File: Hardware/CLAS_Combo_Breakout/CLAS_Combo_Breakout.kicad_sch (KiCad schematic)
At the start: 86 parts, among them J1 USB_C_Receptacle_USB2.0, J2 ZED, J3 NEO, J4 USB_C_Receptacle_USB2.0, J5 Conn_SMA, U1 USBLC6-2P6, U10 NT1191GEAE3S, U2 ZED-F9P, U3 NEO-D9C-00B, U4 USBLC6-2P6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

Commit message: 部品配置を調整
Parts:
- JP1: footprint Jumper:SolderJumper-3_P1.3mm_Open_RoundedPad1.0x1.5mm_NumberLabels -> Jumper_extlib:SolderJumper-3_Open_RoundedPad
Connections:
- net D+ZED: now also U1.6 (I/O1); no longer U1.4 (I/O2)
- net D-ZED: now also U1.4 (I/O2); no longer U1.6 (I/O1)
- net RXD1_ZED: now also J2.6 (Pin_6); no longer J2.5 (Pin_5)
- net TXD1_ZED: now also J2.7 (Pin_7); no longer J2.6 (Pin_6)
- net TX_RDY: now also J2.5 (Pin_5); no longer J2.7 (Pin_7)
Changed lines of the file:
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@@
   (junction (at 43.18 160.02) (diameter 0) (color 0 0 0 0)
   )
-  (junction (at 264.16 43.18) (diameter 0) (color 0 0 0 0)
-  )
   (junction (at 242.57 144.78) (diameter 0) (color 0 0 0 0)
   )
@@
   (junction (at 267.97 144.78) (diameter 0) (color 0 0 0 0)
   )
+  (junction (at 264.16 40.64) (diameter 0) (color 0 0 0 0)
+  )
   (junction (at 35.56 40.64) (diameter 0) (color 0 0 0 0)
   )
+  (junction (at 256.54 43.18) (diameter 0) (color 0 0 0 0)
+  )
   (junction (at 283.21 85.09) (diameter 0) (color 0 0 0 0)
   )
@@
   (junction (at 133.35 68.58) (diameter 0) (color 0 0 0 0)
   )
-  (junction (at 256.54 40.64) (diameter 0) (color 0 0 0 0)
-  )
   (junction (at 267.97 154.94) (diameter 0) (color 0 0 0 0)
   )
@@
     (stroke (width 0) (type default) (color 0 0 0 0))
   )
-  (wire (pts (xy 264.16 43.18) (xy 264.16 44.45))
-    (stroke (width 0) (type default) (color 0 0 0 0))
-  )
   (wire (pts (xy 267.97 144.78) (xy 267.97 147.32))
     (stroke (width 0) (type default) (color 0 0 0 0))
@@
     (stroke (width 0) (type default) (color 0 0 0 0))
   )
+  (wire (pts (xy 256.54 43.18) (xy 256.54 44.45))
+    (stroke (width 0) (type default) (color 0 0 0 0))
+  )
+  (wire (pts (xy 264.16 40.64) (xy 266.7 40.64))
+    (stroke (width 0) (type default) (color 0 0 0 0))
+  )
   (wire (pts (xy 95.25 187.96) (xy 95.25 189.23))
     (stroke (width 0) (type default) (color 0 0 0 0))
@@
     (stroke (width 0) (type default) (color 0 0 0 0))
   )
-  (wire (pts (xy 251.46 43.18) (xy 264.16 43.18))
-    (stroke (width 0) (type default) (color 0 0 0 0))
-  )
   (wire (pts (xy 107.95 165.1) (xy 107.95 172.72))
     (stroke (width 0) (type default) (color 0 0 0 0))
@@
     (stroke (width 0) (type default) (color 0 0 0 0))
   )
-  (wire (pts (xy 264.16 43.18) (xy 266.7 43.18))
+  (wire (pts (xy 251.46 43.18) (xy 256.54 43.18))
     (stroke (width 0) (type default) (color 0 0 0 0))
   )
@@
     (stroke (width 0) (type default) (color 0 0 0 0))
   )
-  (wire (pts (xy 251.46 40.64) (xy 256.54 40.64))
+  (wire (pts (xy 251.46 40.64) (xy 264.16 40.64))
     (stroke (width 0) (type default) (color 0 0 0 0))
   )
@@
     (stroke (width 0) (type default) (color 0 0 0 0))
   )
+  (wire (pts (xy 256.54 43.18) (xy 266.7 43.18))
+    (stroke (width 0) (type default) (color 0 0 0 0))
+  )
   (wire (pts (xy 66.04 144.78) (xy 68.58 144.78))
     (stroke (width 0) (type default) (color 0 0 0 0))
@@
     (stroke (width 0) (type default) (color 0 0 0 0))
   )
-  (wire (pts (xy 256.54 40.64) (xy 266.7 40.64))
-    (stroke (width 0) (type default) (color 0 0 0 0))
-  )
   (wire (pts (xy 35.56 40.64) (xy 35.56 39.37))
     (stroke (width 0) (type default) (color 0 0 0 0))
@@
     (stroke (width 0) (type default) (color 0 0 0 0))
   )
+  (wire (pts (xy 264.16 40.64) (xy 264.16 44.45))
+    (stroke (width 0) (type default) (color 0 0 0 0))
+  )
   (wire (pts (xy 64.77 177.8) (xy 67.31 177.8))
     (stroke (width 0) (type default) (color 0 0 0 0))
@@
     (stroke (width 0) (type default) (color 0 0 0 0))
   )
-  (wire (pts (xy 256.54 40.64) (xy 256.54 44.45))
-    (stroke (width 0) (type default) (color 0 0 0 0))
-  )
   (wire (pts (xy 260.35 92.71) (xy 260.35 99.06))
     (stroke (width 0) (type default) (color 0 0 0 0))
@@
     (effects (font (size 1.27 1.27)) (justify right bottom))
   )
-  (label "TX_RDY" (at 177.8 77.47 180)
+  (label "TX_RDY" (at 177.8 72.39 180)
     (effects (font (size 1.27 1.27)) (justify right bottom))
   )
@@
     (effects (font (size 1.27 1.27)) (justify right bottom))
   )
-  (label "RXD1_ZED" (at 177.8 72.39 180)
+  (label "RXD1_ZED" (at 177.8 74.93 180)
     (effects (font (size 1.27 1.27)) (justify right bottom))
   )
@@
     (effects (font (size 1.27 1.27)) (justify left bottom))
   )
-  (label "TXD1_ZED" (at 177.8 74.93 180)
+  (label "TXD1_ZED" (at 177.8 77.47 180)
     (effects (font (size 1.27 1.27)) (justify right bottom))
   )
@@
     (property "Reference" "JP1" (id 0) (at 121.92 34.29 0))
     (property "Value" "I2C" (id 1) (at 121.92 31.75 0))
-    (property "Footprint" "Jumper:SolderJumper-3_P1.3mm_Open_RoundedPad1.0x1.5mm_NumberLabels" (id 2) (at 121.92 29.21 0)
+    (property "Footprint" "Jumper_extlib:SolderJumper-3_Open_RoundedPad" (id 2) (at 121.92 29.21 0)
       (effects (font (size 1.27 1.27)) hide)
     )
@@
     )
     (path "/b54126b3-7985-4549-85a9-fc253ef56032"
-      (reference "JP1") (unit 1) (value "I2C") (footprint "Jumper:SolderJumper-3_P1.3mm_Open_RoundedPad1.0x1.5mm_NumberLabels")
+      (reference "JP1") (unit 1) (value "I2C") (footprint "Jumper_extlib:SolderJumper-3_Open_RoundedPad")
     )
     (path "/be16f664-0619-4856-937a-e239b591adad"

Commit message: 配線中
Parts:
- removed C9: 0.1u, Capacitor_SMD:C_0603_1608Metric, symbol Device:C_Small
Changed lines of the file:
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@@
   (junction (at 40.64 190.5) (diameter 0) (color 0 0 0 0)
   )
-  (junction (at 267.97 144.78) (diameter 0) (color 0 0 0 0)
-  )
   (junction (at 264.16 40.64) (diameter 0) (color 0 0 0 0)
   )
@@
   (junction (at 133.35 68.58) (diameter 0) (color 0 0 0 0)
   )
-  (junction (at 267.97 154.94) (diameter 0) (color 0 0 0 0)
-  )
   (junction (at 251.46 97.79) (diameter 0) (color 0 0 0 0)
   )
@@
     (stroke (width 0) (type default) (color 0 0 0 0))
   )
-  (wire (pts (xy 267.97 152.4) (xy 267.97 154.94))
-    (stroke (width 0) (type default) (color 0 0 0 0))
-  )
   (wire (pts (xy 43.18 175.26) (xy 43.18 172.72))
     (stroke (width 0) (type default) (color 0 0 0 0))
@@
     (stroke (width 0) (type default) (color 0 0 0 0))
   )
-  (wire (pts (xy 267.97 144.78) (xy 267.97 147.32))
-    (stroke (width 0) (type default) (color 0 0 0 0))
-  )
   (wire (pts (xy 85.09 175.26) (xy 83.82 175.26))
     (stroke (width 0) (type default) (color 0 0 0 0))
@@
     (stroke (width 0) (type default) (color 0 0 0 0))
   )
-  (wire (pts (xy 260.35 144.78) (xy 267.97 144.78))
-    (stroke (width 0) (type default) (color 0 0 0 0))
-  )
   (wire (pts (xy 34.29 66.04) (xy 38.1 66.04))
     (stroke (width 0) (type default) (color 0 0 0 0))
@@
     (stroke (width 0) (type default) (color 0 0 0 0))
   )
-  (wire (pts (xy 260.35 154.94) (xy 267.97 154.94))
+  (wire (pts (xy 260.35 154.94) (xy 269.24 154.94))
     (stroke (width 0) (type default) (color 0 0 0 0))
   )
@@
     (stroke (width 0) (type default) (color 0 0 0 0))
   )
-  (wire (pts (xy 267.97 154.94) (xy 269.24 154.94))
-    (stroke (width 0) (type default) (color 0 0 0 0))
-  )
   (wire (pts (xy 264.16 97.79) (xy 266.7 97.79))
     (stroke (width 0) (type default) (color 0 0 0 0))
@@
     (stroke (width 0) (type default) (color 0 0 0 0))
   )
-  (wire (pts (xy 267.97 144.78) (xy 269.24 144.78))
+  (wire (pts (xy 260.35 144.78) (xy 269.24 144.78))
     (stroke (width 0) (type default) (color 0 0 0 0))
   )
@@
     (pin "2")
   )
-  (symbol (lib_id "Device:C_Small") (at 267.97 149.86 0) (unit 1)
-    (in_bom yes) (on_board yes)
-    (property "Reference" "C9" (id 0) (at 264.16 148.59 0)
-      (effects (font (size 1.27 1.27)) (justify left))
-    )
-    (property "Value" "0.1u" (id 1) (at 262.89 151.13 0)
-      (effects (font (size 1.27 1.27)) (justify left))
-    )
-    (property "Footprint" "Capacitor_SMD:C_0603_1608Metric" (id 2) (at 267.97 149.86 0)
-      (effects (font (size 1.27 1.27)) hide)
-    )
-    (property "Datasheet" "~" (id 3) (at 267.97 149.86 0)
-      (effects (font (size 1.27 1.27)) hide)
-    )
-    (pin "1")
-    (pin "2")
-  )
   (symbol (lib_id "power_extlib:+3.3V_RF") (at 59.69 138.43 0) (unit 1)
     (in_bom no) (on_board no)
@@
       (reference "C8") (unit 1) (value "1u") (footprint "Capacitor_SMD:C_0603_1608Metric")
     )
-    (path "/d9e02dd6-6056-42f6-a336-6b458fa45150"
-      (reference "C9") (unit 1) (value "0.1u") (footprint "Capacitor_SMD:C_0603_1608Metric")
-    )
     (path "/fdc92199-aa87-4c9d-967d-f186d49dc37e"

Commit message: 伝送線路配線完了
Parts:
- added C9: DNF, Capacitor_SMD:C_0603_1608Metric, symbol Device:C_Small
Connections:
- net GND: now also C9.2
- net at C13.2, R31.1: now also C9.1
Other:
- moved on the sheet: ANT1, C13, C16, R33, R34

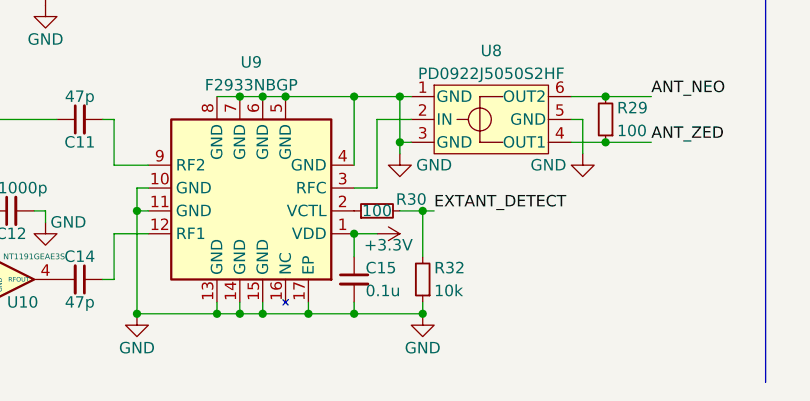
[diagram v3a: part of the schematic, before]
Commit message: プルダウンRをプルアップRに変更、EANTのLEDを移動
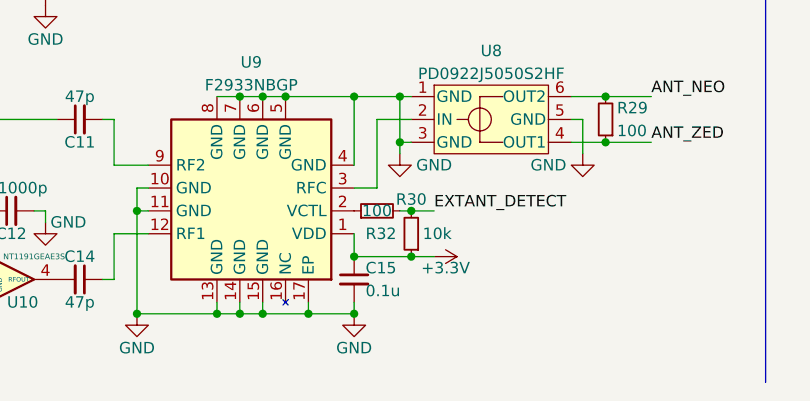
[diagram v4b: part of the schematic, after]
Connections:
- net +3.3V: now also R32.1
- net GND: no longer R32.1
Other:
- moved on the sheet: R32
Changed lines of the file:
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@@
   (junction (at 39.37 191.77) (diameter 0) (color 0 0 0 0)
   )
-  (junction (at 115.57 177.8) (diameter 0) (color 0 0 0 0)
-  )
   (junction (at 135.89 165.1) (diameter 0) (color 0 0 0 0)
   )
@@
   (junction (at 29.21 20.32) (diameter 0) (color 0 0 0 0)
   )
-  (junction (at 107.95 180.34) (diameter 0) (color 0 0 0 0)
-  )
   (junction (at 43.18 153.67) (diameter 0) (color 0 0 0 0)
   )
@@
   (junction (at 59.69 143.51) (diameter 0) (color 0 0 0 0)
   )
+  (junction (at 114.3 182.88) (diameter 0) (color 0 0 0 0)
+  )
   (junction (at 260.35 154.94) (diameter 0) (color 0 0 0 0)
   )
@@
   (junction (at 250.19 154.94) (diameter 0) (color 0 0 0 0)
   )
-  (junction (at 115.57 189.23) (diameter 0) (color 0 0 0 0)
-  )
   (junction (at 95.25 165.1) (diameter 0) (color 0 0 0 0)
   )
@@
   (junction (at 36.83 190.5) (diameter 0) (color 0 0 0 0)
   )
+  (junction (at 107.95 182.88) (diameter 0) (color 0 0 0 0)
+  )
   (junction (at 264.16 40.64) (diameter 0) (color 0 0 0 0)
   )
@@
   )
   (junction (at 251.46 43.18) (diameter 0) (color 0 0 0 0)
+  )
+  (junction (at 114.3 177.8) (diameter 0) (color 0 0 0 0)
   )
   (junction (at 133.35 68.58) (diameter 0) (color 0 0 0 0)
@@
     (stroke (width 0) (type default) (color 0 0 0 0))
   )
-  (wire (pts (xy 107.95 180.34) (xy 110.49 180.34))
-    (stroke (width 0) (type default) (color 0 0 0 0))
-  )
   (wire (pts (xy 33.02 55.88) (xy 35.56 55.88))
     (stroke (width 0) (type default) (color 0 0 0 0))
@@
     (stroke (width 0) (type default) (color 0 0 0 0))
   )
-  (wire (pts (xy 107.95 189.23) (xy 115.57 189.23))
-    (stroke (width 0) (type default) (color 0 0 0 0))
-  )
   (wire (pts (xy 72.39 177.8) (xy 73.66 177.8))
     (stroke (width 0) (type default) (color 0 0 0 0))
@@
     (stroke (width 0) (type default) (color 0 0 0 0))
   )
+  (wire (pts (xy 114.3 177.8) (xy 116.84 177.8))
+    (stroke (width 0) (type default) (color 0 0 0 0))
+  )
   (wire (pts (xy 49.53 160.02) (xy 49.53 158.75))
     (stroke (width 0) (type default) (color 0 0 0 0))
@@
     (stroke (width 0) (type default) (color 0 0 0 0))
   )
-  (wire (pts (xy 115.57 177.8) (xy 116.84 177.8))
-    (stroke (width 0) (type default) (color 0 0 0 0))
-  )
   (wire (pts (xy 73.66 177.8) (xy 73.66 179.07))
     (stroke (width 0) (type default) (color 0 0 0 0))
@@
     (stroke (width 0) (type default) (color 0 0 0 0))
   )
+  (wire (pts (xy 114.3 182.88) (xy 116.84 182.88))
+    (stroke (width 0) (type default) (color 0 0 0 0))
+  )
   (wire (pts (xy 130.81 76.2) (xy 133.35 76.2))
     (stroke (width 0) (type default) (color 0 0 0 0))
@@
     (stroke (width 0) (type default) (color 0 0 0 0))
   )
-  (wire (pts (xy 113.03 177.8) (xy 115.57 177.8))
+  (wire (pts (xy 113.03 177.8) (xy 114.3 177.8))
     (stroke (width 0) (type default) (color 0 0 0 0))
   )
@@
     (stroke (width 0) (type default) (color 0 0 0 0))
   )
+  (wire (pts (xy 107.95 182.88) (xy 114.3 182.88))
+    (stroke (width 0) (type default) (color 0 0 0 0))
+  )
   (wire (pts (xy 260.35 92.71) (xy 260.35 99.06))
     (stroke (width 0) (type default) (color 0 0 0 0))
@@
     (stroke (width 0) (type default) (color 0 0 0 0))
   )
-  (wire (pts (xy 115.57 177.8) (xy 115.57 182.88))
-    (stroke (width 0) (type default) (color 0 0 0 0))
-  )
   (wire (pts (xy 35.56 63.5) (xy 35.56 55.88))
     (stroke (width 0) (type default) (color 0 0 0 0))
@@
   )
   (wire (pts (xy 31.75 185.42) (xy 39.37 185.42))
-    (stroke (width 0) (type default) (color 0 0 0 0))
-  )
-  (wire (pts (xy 115.57 187.96) (xy 115.57 189.23))
     (stroke (width 0) (type default) (color 0 0 0 0))
   )
@@
     (pin "2")
   )
-  (symbol (lib_id "power:GND") (at 115.57 189.23 0) (mirror y) (unit 1)
-    (in_bom yes) (on_board yes)
-    (property "Reference" "#PWR044" (id 0) (at 115.57 195.58 0)
-      (effects (font (size 1.27 1.27)) hide)
-    )
-    (property "Value" "GND" (id 1) (at 115.57 193.04 0))
-    (property "Footprint" "" (id 2) (at 115.57 189.23 0)
-      (effects (font (size 1.27 1.27)) hide)
-    )
-    (property "Datasheet" "" (id 3) (at 115.57 189.23 0)
+  (symbol (lib_id "power:GND") (at 107.95 189.23 0) (mirror y) (unit 1)
+    (in_bom yes) (on_board yes)
+    (property "Reference" "#PWR044" (id 0) (at 107.95 195.58 0)
+      (effects (font (size 1.27 1.27)) hide)
+    )
+    (property "Value" "GND" (id 1) (at 107.95 193.04 0))
+    (property "Footprint" "" (id 2) (at 107.95 189.23 0)
+      (effects (font (size 1.27 1.27)) hide)
+    )
+    (property "Datasheet" "" (id 3) (at 107.95 189.23 0)
       (effects (font (size 1.27 1.27)) hide)
     )
@@
     (pin "1")
   )
-  (symbol (lib_id "power:+3.3V") (at 110.49 180.34 270) (unit 1)
-    (in_bom yes) (on_board yes)
-    (property "Reference" "#PWR042" (id 0) (at 106.68 180.34 0)
-      (effects (font (size 1.27 1.27)) hide)
-    )
-    (property "Value" "+3.3V" (id 1) (at 111.76 181.61 90))
-    (property "Footprint" "" (id 2) (at 110.49 180.34 0)
-      (effects (font (size 1.27 1.27)) hide)
-    )
-    (property "Datasheet" "" (id 3) (at 110.49 180.34 0)
+  (symbol (lib_id "power:+3.3V") (at 116.84 182.88 270) (unit 1)
+    (in_bom yes) (on_board yes)
+    (property "Reference" "#PWR042" (id 0) (at 113.03 182.88 0)
+      (effects (font (size 1.27 1.27)) hide)
+    )
+    (property "Value" "+3.3V" (id 1) (at 118.11 184.15 90))
+    (property "Footprint" "" (id 2) (at 116.84 182.88 0)
+      (effects (font (size 1.27 1.27)) hide)
+    )
+    (property "Datasheet" "" (id 3) (at 116.84 182.88 0)
       (effects (font (size 1.27 1.27)) hide)
     )
@@
     (pin "9")
   )
-  (symbol (lib_id "Device:R_Small") (at 115.57 185.42 180) (unit 1)
-    (in_bom yes) (on_board yes)
-    (property "Reference" "R32" (id 0) (at 116.84 184.15 0)
+  (symbol (lib_id "Device:R_Small") (at 114.3 180.34 180) (unit 1)
+    (in_bom yes) (on_board yes)
+    (property "Reference" "R32" (id 0) (at 109.22 180.34 0)
       (effects (font (size 1.27 1.27)) (justify right))
     )
-    (property "Value" "10k" (id 1) (at 116.84 186.69 0)
+    (property "Value" "10k" (id 1) (at 115.57 180.34 0)
       (effects (font (size 1.27 1.27)) (justify right))
     )
-    (property "Footprint" "Resistor_SMD:R_0603_1608Metric" (id 2) (at 115.57 185.42 0)
-      (effects (font (size 1.27 1.27)) hide)
-    )
-    (property "Datasheet" "~" (id 3) (at 115.57 185.42 0)
-      (effects (font (size 1.27 1.27)) hide)
-    )
+    (property "Footprint" "Resistor_SMD:R_0603_1608Metric" (id 2) (at 114.3 180.34 0)
+      (effects (font (size 1.27 1.27)) hide)
+    )
+    (property "Datasheet" "~" (id 3) (at 114.3 180.34 0)
+      (effects (font (size 1.27 1.27)) hide)
+    )

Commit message: アンテナのFootprintをデータシートに準拠
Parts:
- C11, C13, C14, C16, C9: footprint Capacitor_SMD:C_0603_1608Metric -> Capacitor_SMD:C_0402_1005Metric
- R31, R33, R34: footprint Resistor_SMD:R_0603_1608Metric -> Resistor_SMD:R_0402_1005Metric
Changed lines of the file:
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@@
     (property "Reference" "R33" (id 0) (at 34.29 185.42 90))
     (property "Value" "0" (id 1) (at 34.29 187.96 90))
-    (property "Footprint" "Resistor_SMD:R_0603_1608Metric" (id 2) (at 34.29 187.96 0)
+    (property "Footprint" "Resistor_SMD:R_0402_1005Metric" (id 2) (at 34.29 187.96 0)
       (effects (font (size 1.27 1.27)) hide)
     )
@@
     (property "Reference" "R34" (id 0) (at 34.29 193.04 90))
     (property "Value" "0" (id 1) (at 34.29 190.5 90))
-    (property "Footprint" "Resistor_SMD:R_0603_1608Metric" (id 2) (at 34.29 190.5 0)
+    (property "Footprint" "Resistor_SMD:R_0402_1005Metric" (id 2) (at 34.29 190.5 0)
       (effects (font (size 1.27 1.27)) hide)
     )
@@
       (effects (font (size 1.27 1.27)) (justify left))
     )
-    (property "Footprint" "Capacitor_SMD:C_0603_1608Metric" (id 2) (at 39.37 187.96 0)
+    (property "Footprint" "Capacitor_SMD:C_0402_1005Metric" (id 2) (at 39.37 187.96 0)
       (effects (font (size 1.27 1.27)) hide)
     )
@@
       (effects (font (size 1.27 1.27)) (justify left))
     )
-    (property "Footprint" "Capacitor_SMD:C_0603_1608Metric" (id 2) (at 46.99 187.96 0)
+    (property "Footprint" "Capacitor_SMD:C_0402_1005Metric" (id 2) (at 46.99 187.96 0)
       (effects (font (size 1.27 1.27)) hide)
     )
@@
     (property "Reference" "C13" (id 0) (at 43.18 180.34 90))
     (property "Value" "3.9p" (id 1) (at 43.18 182.88 90))
-    (property "Footprint" "Capacitor_SMD:C_0603_1608Metric" (id 2) (at 43.18 185.42 0)
+    (property "Footprint" "Capacitor_SMD:C_0402_1005Metric" (id 2) (at 43.18 185.42 0)
       (effects (font (size 1.27 1.27)) hide)
     )
@@
     (property "Reference" "C14" (id 0) (at 77.47 182.88 90))
     (property "Value" "47p" (id 1) (at 77.47 187.96 90))
-    (property "Footprint" "Capacitor_SMD:C_0603_1608Metric" (id 2) (at 77.47 185.42 0)
+    (property "Footprint" "Capacitor_SMD:C_0402_1005Metric" (id 2) (at 77.47 185.42 0)
       (effects (font (size 1.27 1.27)) hide)
     )
@@
     (property "Reference" "R31" (id 0) (at 52.07 180.34 90))
     (property "Value" "0" (id 1) (at 52.07 182.88 90))
-    (property "Footprint" "Resistor_SMD:R_0603_1608Metric" (id 2) (at 52.07 185.42 0)
+    (property "Footprint" "Resistor_SMD:R_0402_1005Metric" (id 2) (at 52.07 185.42 0)
       (effects (font (size 1.27 1.27)) hide)
     )
@@
     (property "Reference" "C11" (id 0) (at 77.47 170.18 90))
     (property "Value" "47p" (id 1) (at 77.47 165.1 90))
-    (property "Footprint" "Capacitor_SMD:C_0603_1608Metric" (id 2) (at 77.47 167.64 0)
+    (property "Footprint" "Capacitor_SMD:C_0402_1005Metric" (id 2) (at 77.47 167.64 0)
       (effects (font (size 1.27 1.27)) hide)
     )
@@
     )
     (path "/7f3751d8-f78b-48df-9f8b-6242d813763f"
-      (reference "C9") (unit 1) (value "DNF") (footprint "Capacitor_SMD:C_0603_1608Metric")
+      (reference "C9") (unit 1) (value "DNF") (footprint "Capacitor_SMD:C_0402_1005Metric")
     )
     (path "/fdc92199-aa87-4c9d-967d-f186d49dc37e"
@@
     )
     (path "/fbb7695f-2fe9-4673-8b96-4e498f1ce5f5"
-      (reference "C11") (unit 1) (value "47p") (footprint "Capacitor_SMD:C_0603_1608Metric")
+      (reference "C11") (unit 1) (value "47p") (footprint "Capacitor_SMD:C_0402_1005Metric")
     )
     (path "/cd625db1-7e1f-423c-aafc-88b27556b813"
@@
     )
     (path "/867af491-5ec9-4191-b057-5cf560b1f64d"
-      (reference "C13") (unit 1) (value "3.9p") (footprint "Capacitor_SMD:C_0603_1608Metric")
+      (reference "C13") (unit 1) (value "3.9p") (footprint "Capacitor_SMD:C_0402_1005Metric")
     )
     (path "/af52ff3d-dddb-40e9-9ca5-fa9fd5c04d5f"
-      (reference "C14") (unit 1) (value "47p") (footprint "Capacitor_SMD:C_0603_1608Metric")
+      (reference "C14") (unit 1) (value "47p") (footprint "Capacitor_SMD:C_0402_1005Metric")
     )
     (path "/41e1e89a-31bd-44b0-8014-d22389547d82"
@@
     )
     (path "/7e3d3d51-db5e-4db4-96c7-867a851d76fe"
-      (reference "C16") (unit 1) (value "1.2p") (footprint "Capacitor_SMD:C_0603_1608Metric")
+      (reference "C16") (unit 1) (value "1.2p") (footprint "Capacitor_SMD:C_0402_1005Metric")
     )
     (path "/3ff10367-d39a-4d85-9deb-ee015c0a7ef1"
@@
     )
     (path "/ee9f82c2-3335-4a66-9b53-1531ffead520"
-      (reference "R31") (unit 1) (value "0") (footprint "Resistor_SMD:R_0603_1608Metric")
+      (reference "R31") (unit 1) (value "0") (footprint "Resistor_SMD:R_0402_1005Metric")
     )
     (path "/bbfdc1eb-f754-4015-b95e-bafb921ba8ab"
@@
     )
     (path "/0b60f5ea-c267-48a6-b884-b1df458da5ac"
-      (reference "R33") (unit 1) (value "0") (footprint "Resistor_SMD:R_0603_1608Metric")
+      (reference "R33") (unit 1) (value "0") (footprint "Resistor_SMD:R_0402_1005Metric")
     )
     (path "/64668e3a-58f4-4bd8-8bc9-97c90e80e381"
-      (reference "R34") (unit 1) (value "0") (footprint "Resistor_SMD:R_0603_1608Metric")
+      (reference "R34") (unit 1) (value "0") (footprint "Resistor_SMD:R_0402_1005Metric")
     )
     (path "/5cd0f9ce-bd6c-4489-aa98-1c3c6ad64cab"
